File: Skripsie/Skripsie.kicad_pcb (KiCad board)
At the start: 2 copper layers, 180 x 150 mm, 290 parts, among them J1 STM32F4_Discovery, J10 LED_R_TEST, J11 3V3, J12 UART_TEST, J13 USB_B, J2 LCD_TEST, J3 BTN_C_TEST, J4 LED_C_TEST, J5 LED_SER_TEST, J6 BTN_SER_TEST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

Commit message: Update to majority of PCB
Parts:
- C1, C2, J1, J13, POT3, Q1, Q2, R1, R2, R3, R4, R5, U1, U3, U6, U7: moved to B.Cu
- LCD1: footprint Connector_PinHeader_2.54mm:PinHeader_1x16_P2.54mm_Vertical -> pieter:PC1601A
- moved C3 377.3 mm to (26.0, 24.1)
- moved D33 377.3 mm to (22.9, 15.2)
- moved R6 377.3 mm to (26.0, 29.8)
- moved U2 377.3 mm to (14.6, 6.35)
- moved U4 377.3 mm to (26.0, 5.71)
- moved U5 377.3 mm to (14.6, 22.9)
- moved R14 280.7 mm to (208.8, 10.2), turned to 90 degrees
- moved R13 280.2 mm to (205.0, 10.2), turned to 270 degrees
- moved C6 269.7 mm to (186.7, -4.45), turned to 180 degrees
- moved C4 264.9 mm to (176.4, 9.76), turned to 90 degrees
- moved R15 261.7 mm to (168.1, -8.89), turned to 0 degrees
- moved R10 260.5 mm to (172.6, 13.2), turned to 90 degrees
- moved C5 257.4 mm to (168.1, -2.54)
- moved R12 253.7 mm to (172.6, 6.81), turned to 270 degrees
- moved C7 250.4 mm to (168.1, -5.71), turned to 180 degrees
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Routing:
- net bc15: track 44.9 -> 176.1 mm, vias 0 -> 1
- net c0: track 120.8 -> 247.1 mm
- net bc14: track 44.9 -> 167.8 mm, vias 0 -> 1
- net c1: track 120.2 -> 240.5 mm
- net bc13: track 44.9 -> 160.3 mm, vias 0 -> 1
- net r4: track 161.9 -> 276.5 mm, vias 0 -> 1
- net c2: track 120.2 -> 234.1 mm
- net bc12: track 44.9 -> 152.1 mm, vias 0 -> 1
- net c3: track 120.8 -> 227.9 mm
- net USART1_RX: track 0.00 -> 104.1 mm, vias 0 -> 1
- net LCD_E: track 0.00 -> 103.2 mm, vias 0 -> 1
- net c4: track 120.2 -> 220.7 mm
- net bc11: track 44.9 -> 144.2 mm, vias 0 -> 1
- net BTN_R4: track 285.7 -> 384.8 mm, vias 0 -> 1
- net r3: track 163.2 -> 259.3 mm, vias 0 -> 1
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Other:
- board size 180 x 150 mm -> 200 x 165 mm

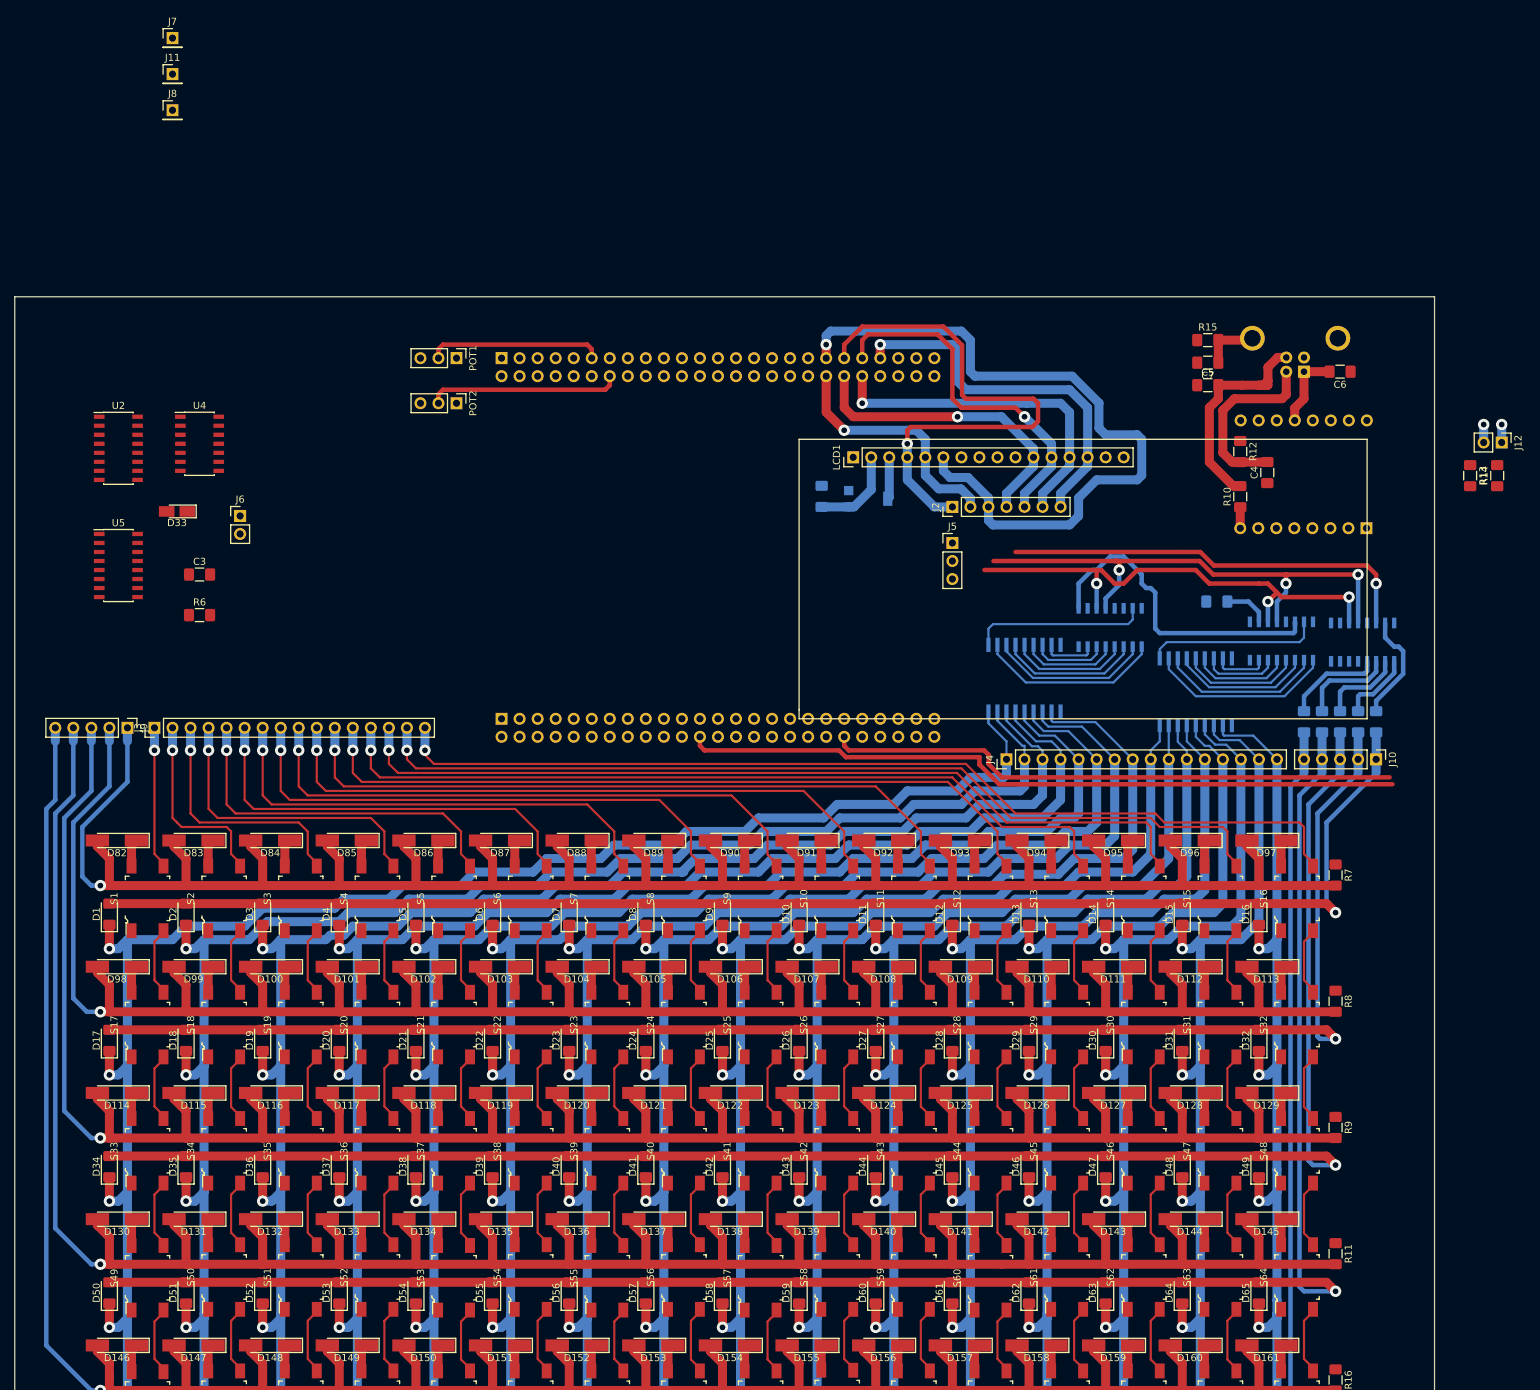
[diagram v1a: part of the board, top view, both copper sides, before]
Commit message: PCB complete before infill
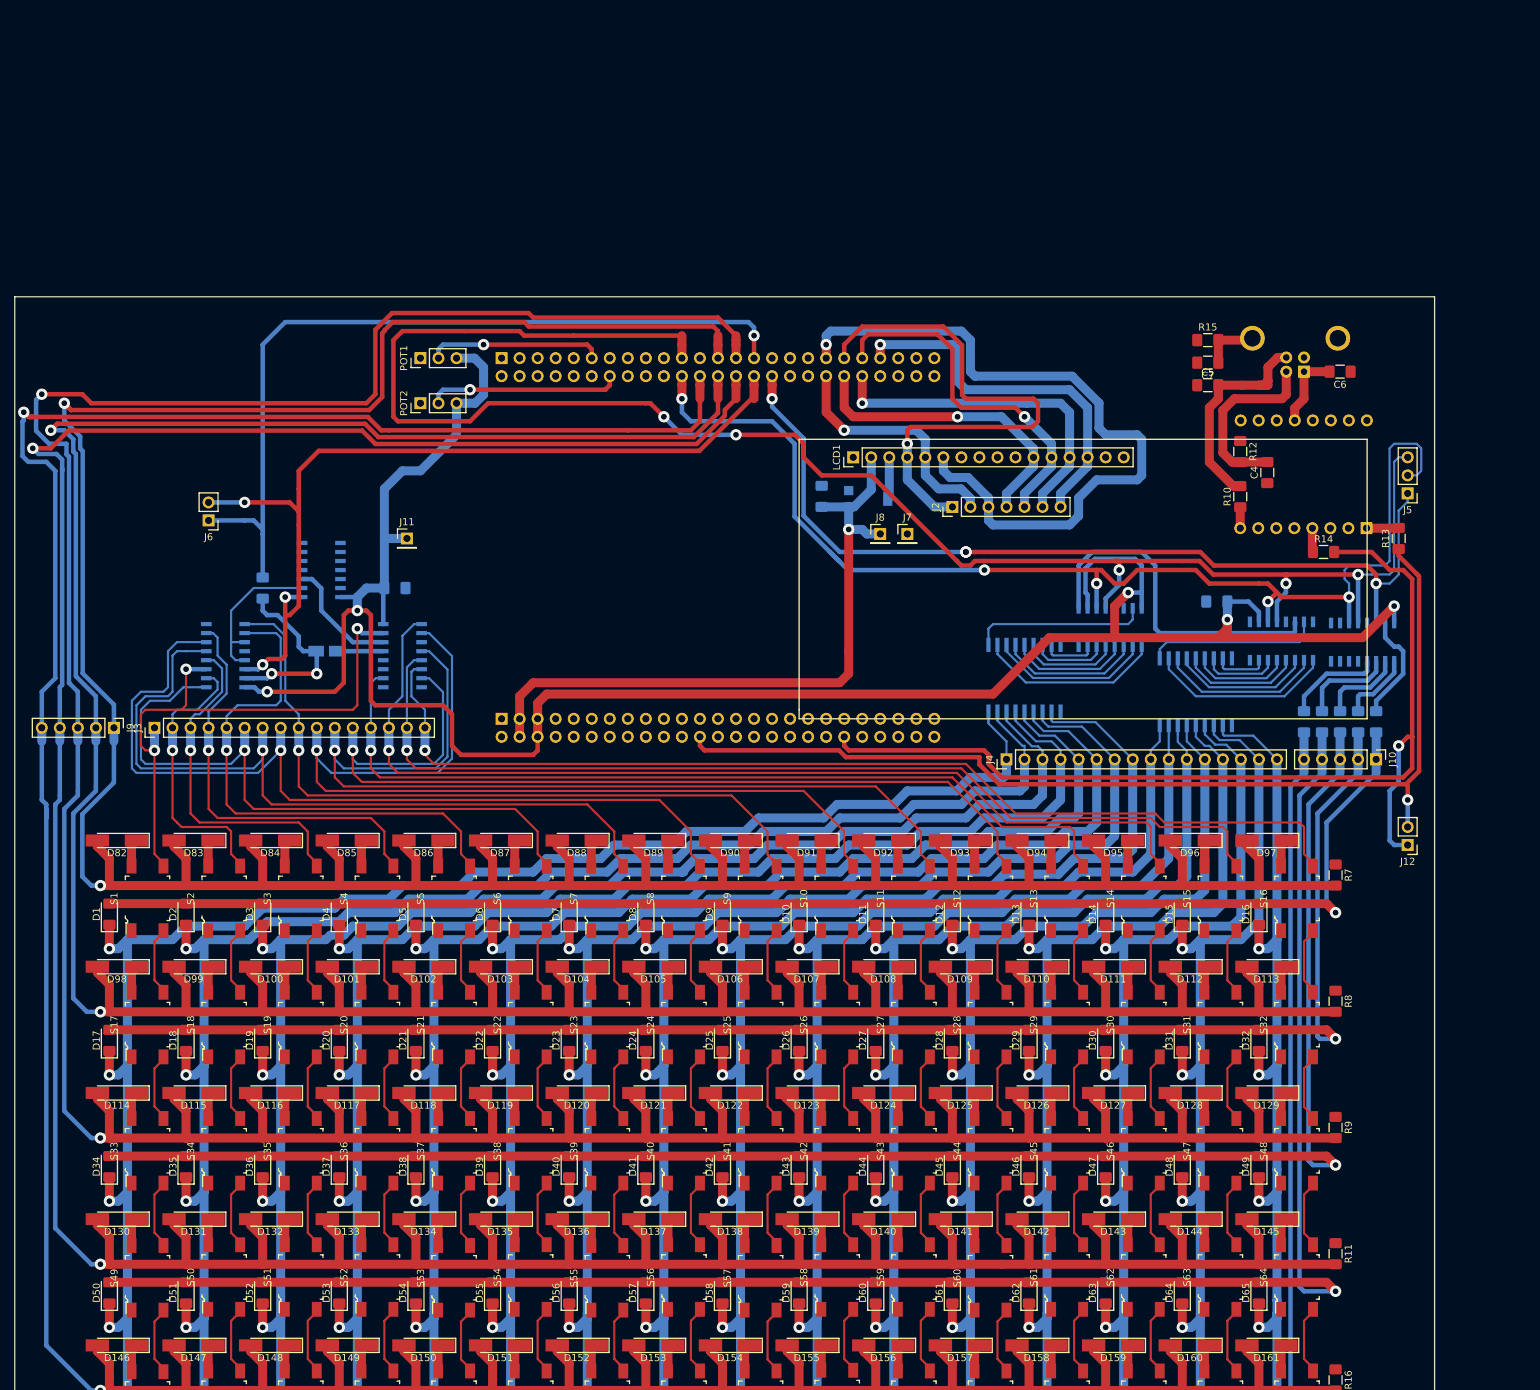
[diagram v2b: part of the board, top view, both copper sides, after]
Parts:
- C3, D33, R6, U2, U4, U5: moved to B.Cu
- moved J7 124.9 mm to (125.7, 18.4)
- moved J8 116.2 mm to (121.9, 18.4)
- moved J11 73.3 mm to (55.2, 19.1)
- moved J5 64.5 mm to (196.2, 12.7), turned to 180 degrees
- moved J12 58.2 mm to (196.2, 62.2), turned to 180 degrees
- moved U5 42.0 mm to (54.6, 35.6), turned to 180 degrees
- moved U2 32.9 mm to (29.7, 35.6)
- moved D33 28.8 mm to (43.9, 34.9)
- moved C3 27.6 mm to (53.6, 26.0)
- moved R14 26.7 mm to (184.4, 21.0), turned to 0 degrees
- moved U4 24.7 mm to (43.2, 23.5)
- moved R13 13.4 mm to (194.9, 19.1), turned to 90 degrees
- moved R6 9.67 mm to (34.9, 26.0), turned to 90 degrees
- moved POT1 5.08 mm to (57.1, -6.35), turned to 90 degrees
- moved POT2 5.08 mm to (57.1, 0.00), turned to 90 degrees
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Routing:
- net +3V3: track 6.44 -> 312.9 mm, vias 0 -> 5
- net LED_RCLK: track 74.2 -> 249.0 mm, vias 3 -> 5
- net BTN_R2: track 350.1 -> 513.9 mm, vias 1 -> 2
- net BTN_R0: track 313.4 -> 469.9 mm, vias 1 -> 2
- net BTN_R4: track 384.8 -> 538.0 mm, vias 1 -> 2
- net BTN_R3: track 367.0 -> 516.5 mm, vias 1 -> 2
- net BTN_R1: track 331.6 -> 479.5 mm, vias 1 -> 2
- net BTN_SRCLK: track 0.00 -> 124.3 mm, vias 0 -> 3
- net BTN_RESET: track 0.00 -> 116.1 mm, vias 0 -> 1
- net LED_SRCLK: track 68.2 -> 171.2 mm, vias 3 -> 5
- net +5V: track 12.5 -> 94.1 mm, vias 0 -> 1
- net LED_SERIAL: track 58.9 -> 128.1 mm, vias 1 -> 4
- net bc0: track 58.7 -> 120.5 mm, vias 1 -> 3
- net USART1_TX: track 83.2 -> 142.7 mm
- net bc7: track 112.7 -> 161.6 mm
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
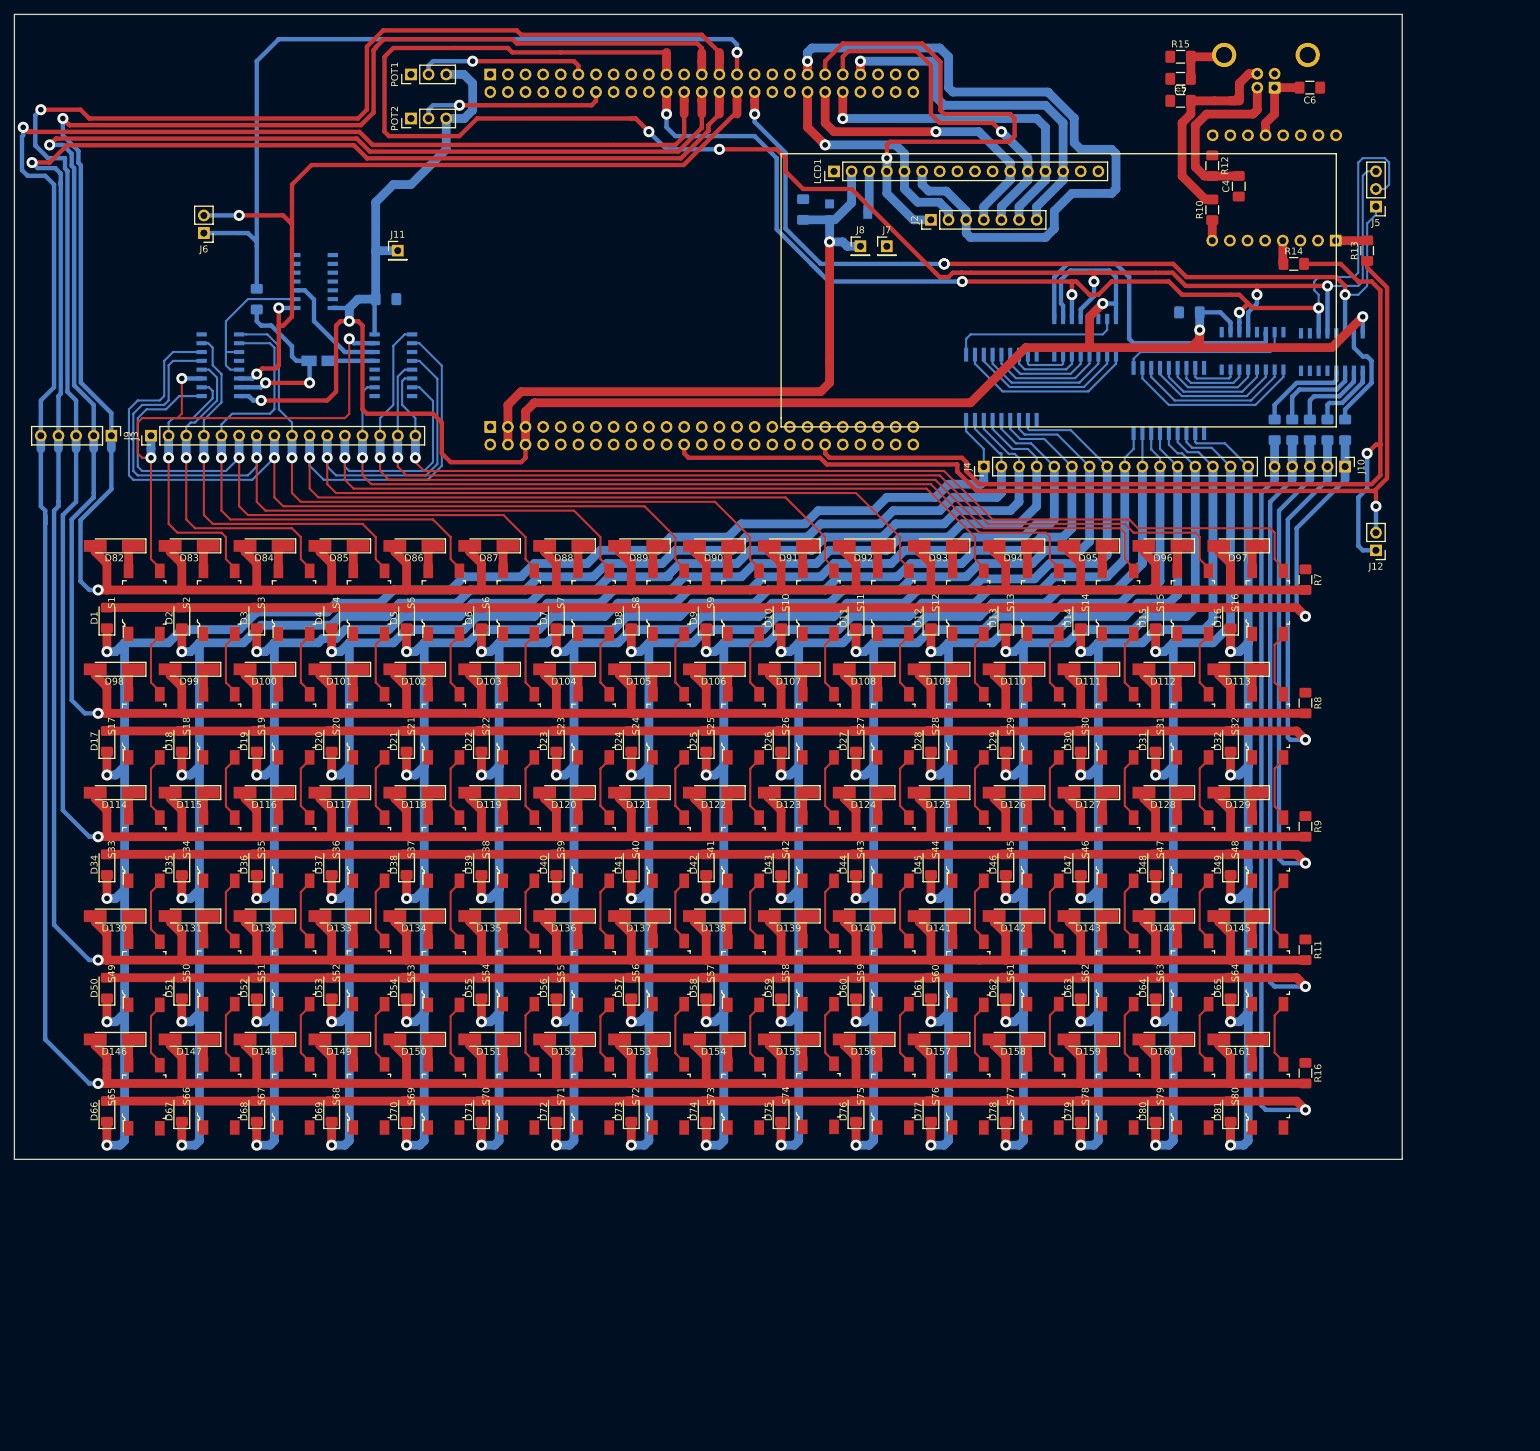
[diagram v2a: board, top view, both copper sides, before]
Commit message: Adjusted traces for more efficiency
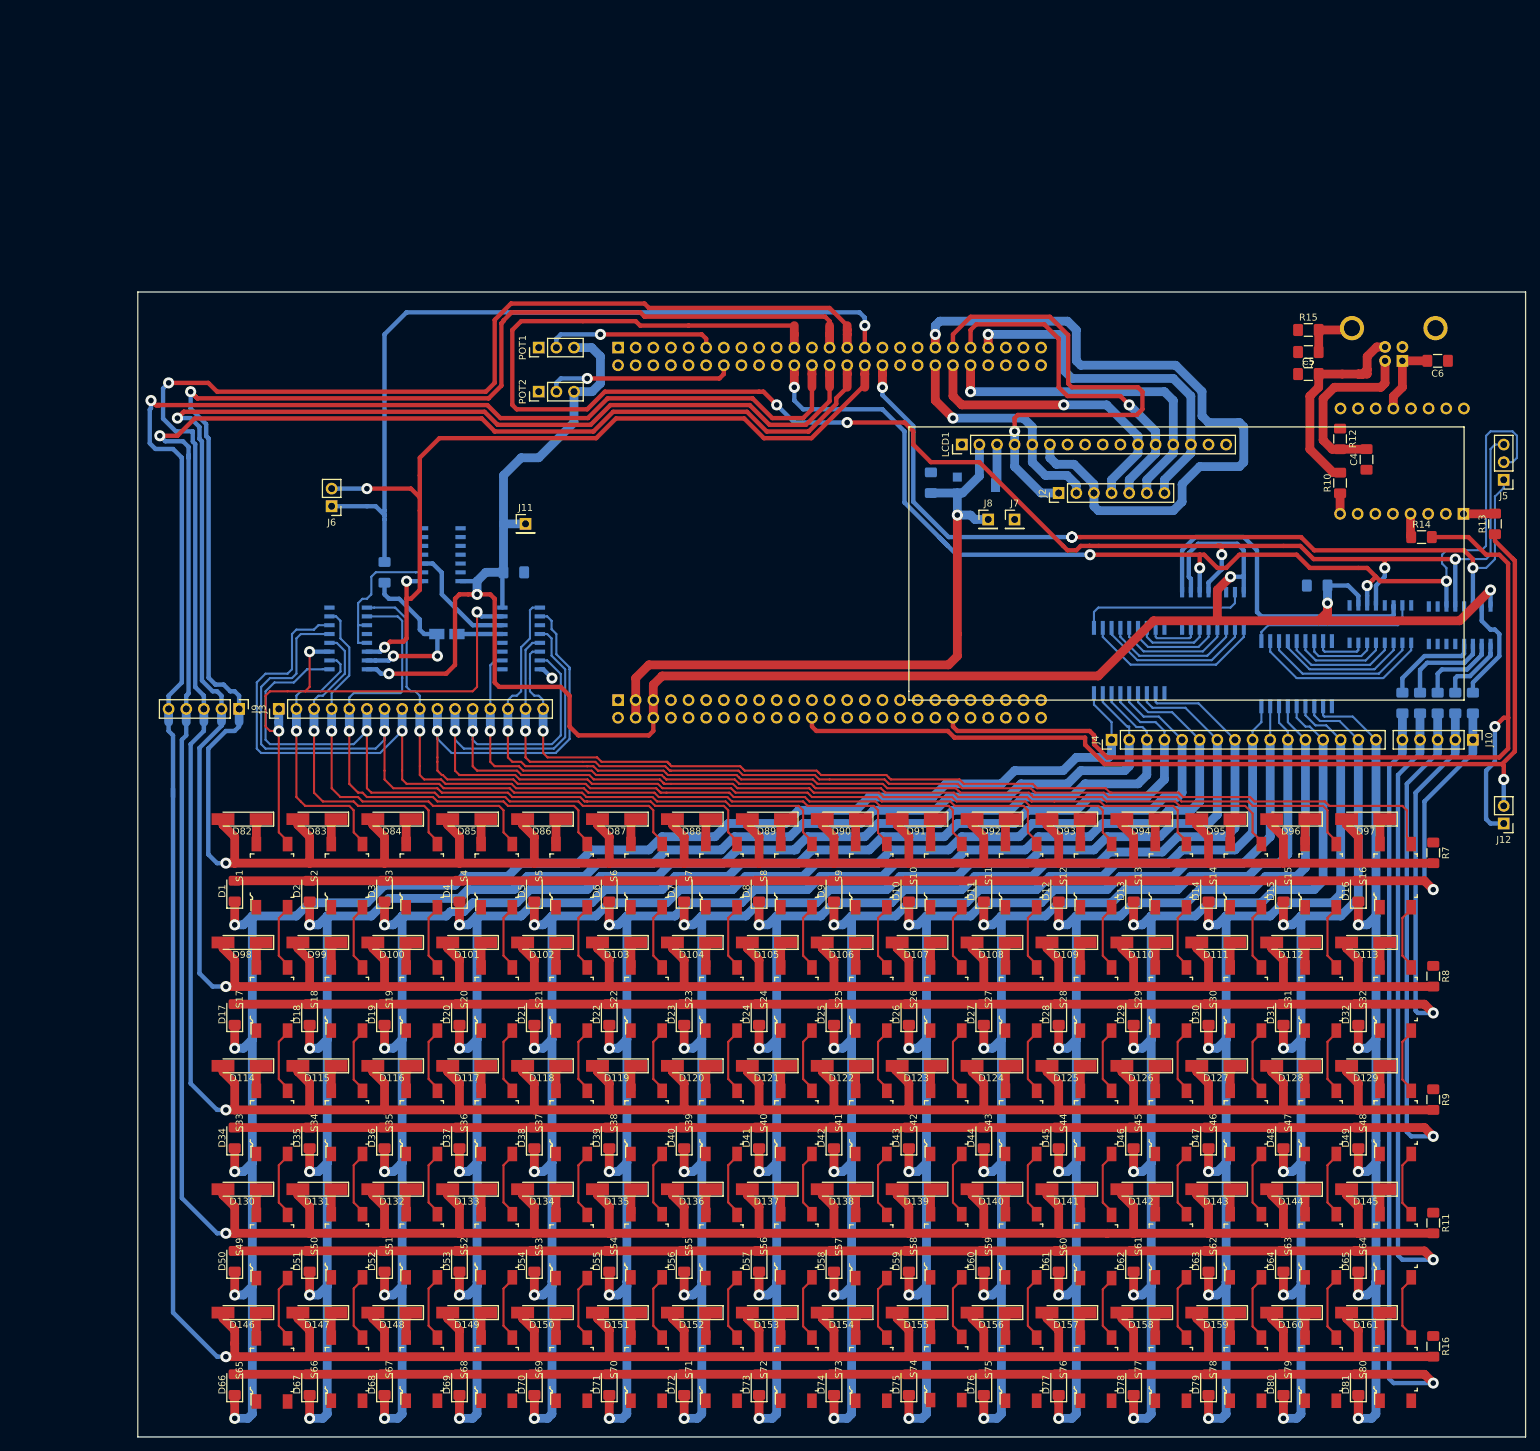
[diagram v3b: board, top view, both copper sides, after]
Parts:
- moved S62 43.5 mm to (177.5, 162.5)
- moved S50 43.5 mm to (47.9, 162.5)
- moved S51 43.5 mm to (58.7, 162.5)
- moved S56 43.5 mm to (112.7, 162.5)
- moved S58 43.5 mm to (134.3, 162.5)
- moved C1 43.5 mm to (187.7, 67.3)
- moved D10 43.5 mm to (128.9, 111.3)
- moved D105 43.5 mm to (108.4, 118.7)
- moved D106 43.5 mm to (119.2, 118.7)
- moved D107 43.5 mm to (130.0, 118.7)
- moved D109 43.5 mm to (151.6, 118.7)
- moved D111 43.5 mm to (173.1, 118.7)
- moved D113 43.5 mm to (194.7, 118.7)
- moved D121 43.5 mm to (108.4, 136.5)
- moved D122 43.5 mm to (119.2, 136.5)
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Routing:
- net BTN_R1: track 479.5 -> 482.2 mm
- net bc15: track 186.4 -> 188.7 mm
- net BTN_R3: track 516.5 -> 518.9 mm
- net BTN_R4: track 538.0 -> 540.4 mm
- net BTN_SRCLK: track 124.3 -> 126.6 mm
- net GND: track 0.00 -> 2.27 mm, vias 0 -> 1
- net BTN_R0: track 469.9 -> 471.7 mm
- net bc12: track 160.4 -> 161.9 mm
- net bc14: track 178.8 -> 180.3 mm
- net bc11: track 171.6 -> 173.0 mm
- net bc8: track 140.7 -> 141.8 mm
- net bc9: track 170.3 -> 171.4 mm
- net bc10: track 171.7 -> 172.8 mm
- net bc13: track 177.5 -> 178.3 mm
- net Net-(U2-Pad11): track 21.7 -> 21.0 mm
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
